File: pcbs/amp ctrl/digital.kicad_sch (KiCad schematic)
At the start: 97 parts, among them J14 RF_Shield_Two_Pieces, U11 LT1880, U12 74LVC1G04, U6 LTC6220/LT6202, U8 AD5676, U90 ADS8168/ADS8167

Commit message: Backplane comms updates, manufacturing renaming
Removed misspelled "maunfacturing" folder, fixed gitignore rule to remove manufacturing folders within individual PCB folders too
Changed SCKI/SCKO terminology to SCK, SCK_LB (loopback) for clarity
Added ADC_CS loopback signal between amp ctrl board & backplane for better fast-clock timing (#38)
Backplane: changed LVDS FPGA outputs to single-ended FPGA outputs to gain more I/O pins, added external LVDS transceivers (#38)
Backplane: replaced global clock & ~LDAC buffers with a separate FPGA pin for each amp ctrl board (#38)
Backplane: removed +2.5V power supply and level translations, no longer needed without FPGA I/O pins using LVDS_25 I/O configuration
Backplane: replaced +VDC-input resistor with solder jumper (on by default)
Backplane: changed field names (Part Number to MPN) to match Aisler's naming convention for automatic recognition
Amp ctrl: fixed optional level-shifter circuit on each channel for voltage inputs (#9) schematic & channel-1 layout
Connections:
- net ADC_SCK_LB: now reaches U12.4, U90.25 (SClk)
- net ADC_SCKI renamed ADC_SCK
- net DAC_SCKI renamed DAC_SCK

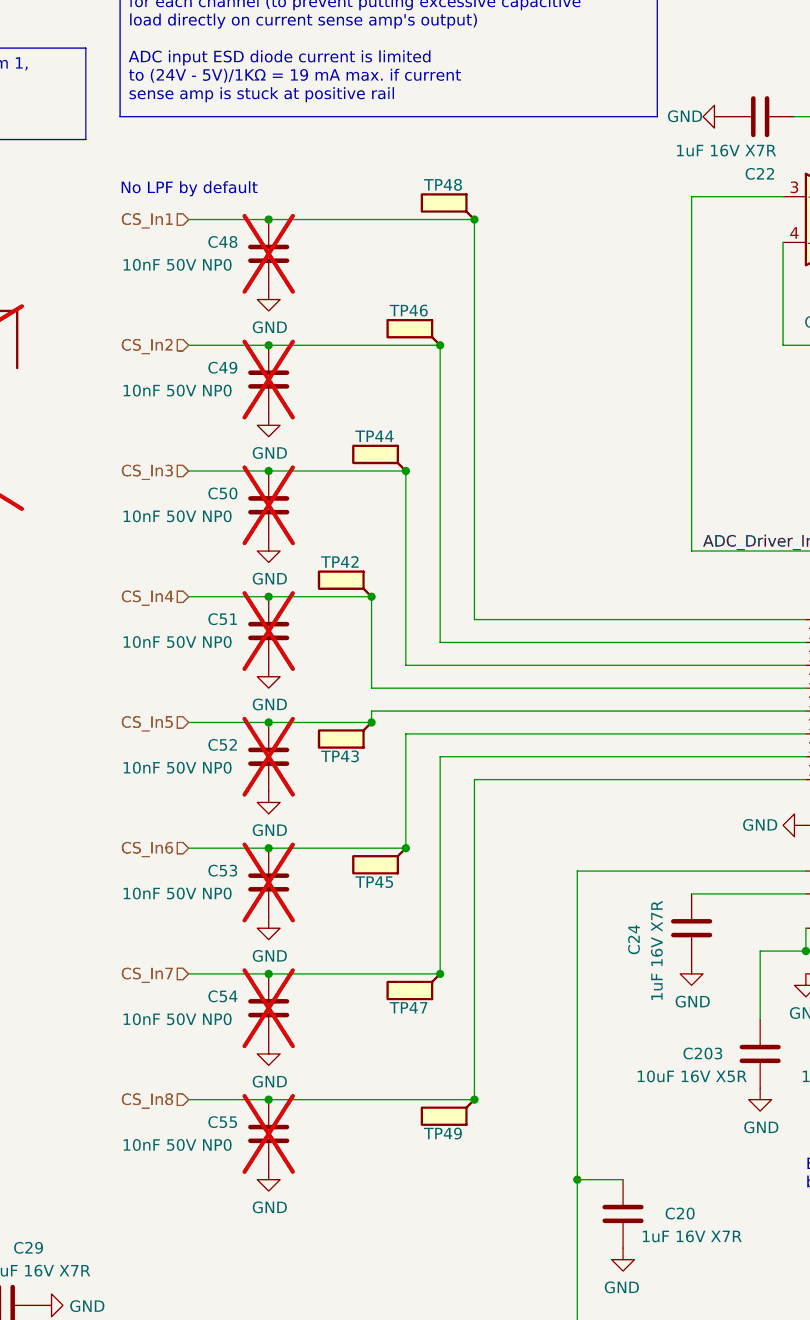
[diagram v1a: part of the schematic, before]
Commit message: Amp control board layout
Finished routing for pinout changes on backplane-to-amp-board connectors (fixes #38)
Changed ADC input testpoints back to pads (from solder-loops), as the Keystone 5019 pads didn't fit, and current sense signals can be probed at the individual channels anyways
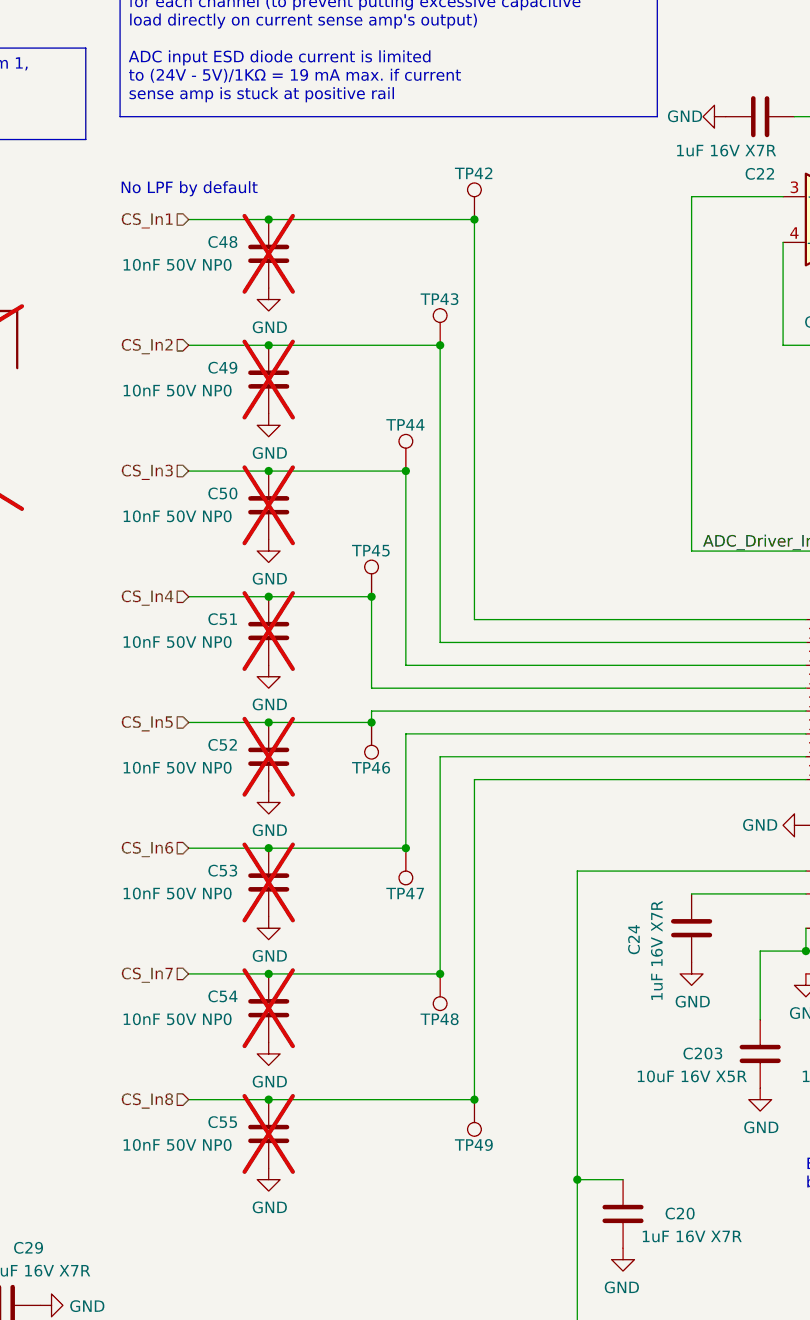
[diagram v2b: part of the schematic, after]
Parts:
- removed TP42, TP43, TP44, TP45, TP46, TP47, TP48, TP49: TestPoint_Flag, TestPoint:TestPoint_Keystone_5019_Miniature, symbol Connector:TestPoint_Flag
- added TP42, TP43, TP44, TP45, TP46, TP47, TP48, TP49: TestPoint, TestPoint:TestPoint_Pad_1.0x1.0mm, symbol Connector:TestPoint
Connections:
- net CS_In1: now also TP42.1
- net CS_In2: now also TP43.1
- net CS_In3: now also TP44.1
- net CS_In4: now also TP45.1
- net CS_In5: now also TP46.1
- net CS_In6: now also TP47.1
- net CS_In7: now also TP48.1
- net CS_In8: now also TP49.1

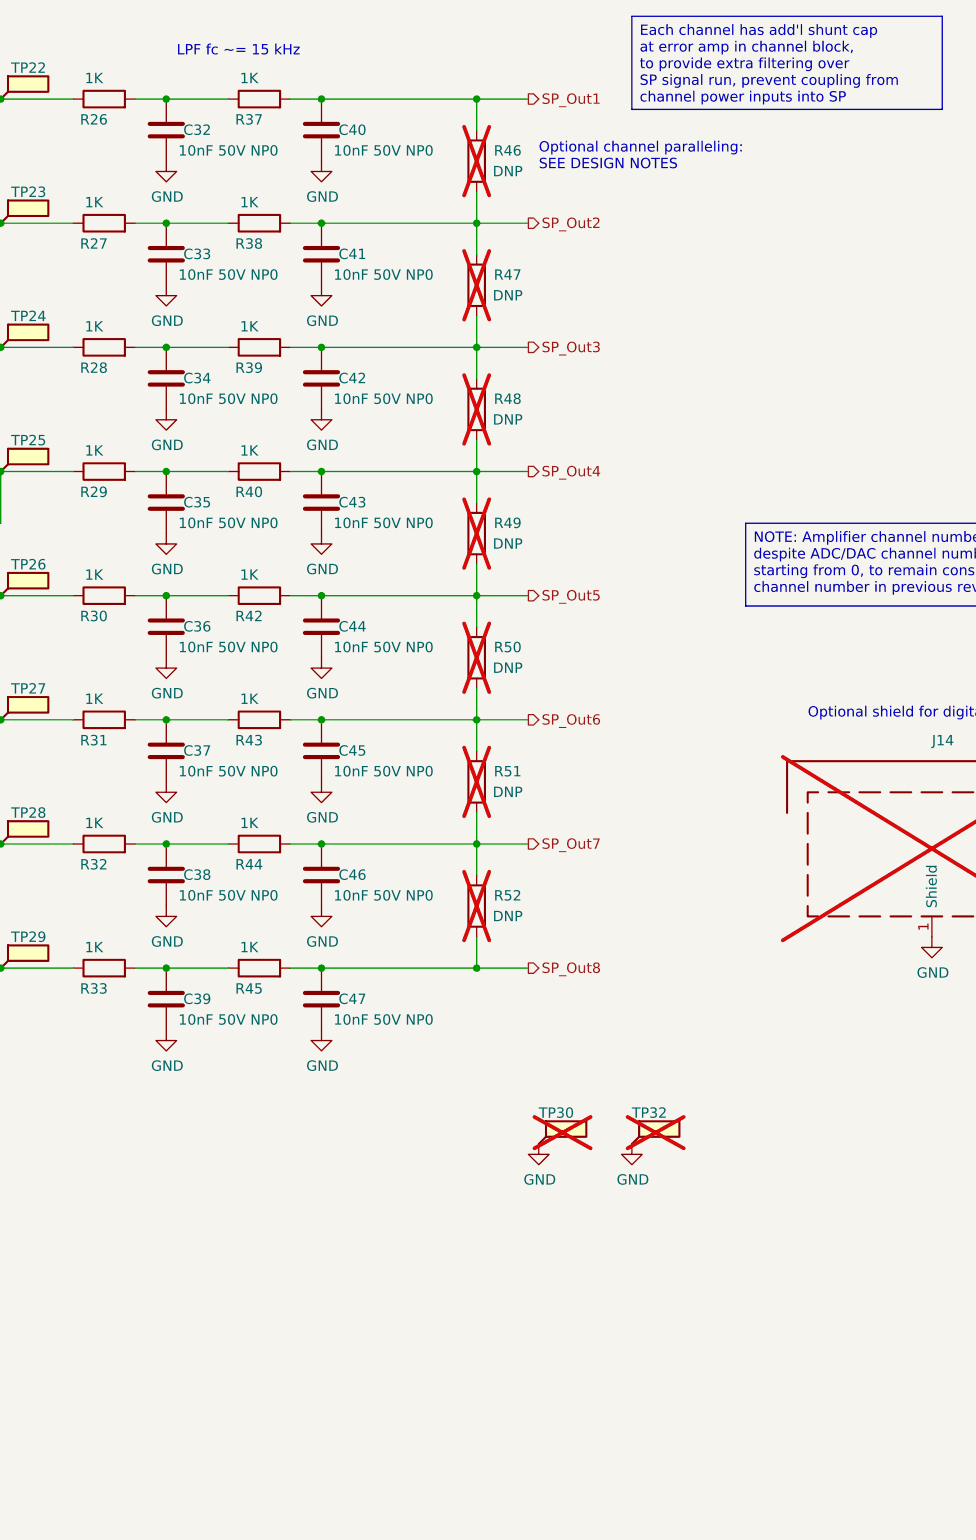
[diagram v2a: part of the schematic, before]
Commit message: Amp ctrl: DAC-filter jumpers, paralleling channels
Added jumpers to disconnect 2nd set of filter capacitors in DAC smoothing filter (fixes #42)
Extended shield footprint around digital section, no longer fits off-the-shelf part (but haven't had a reason to use it yet) to leave room for jumpers
Changed to an experimental channel-paralleling scheme (#19)
Finished copying level shifter layout to other channels (#9)
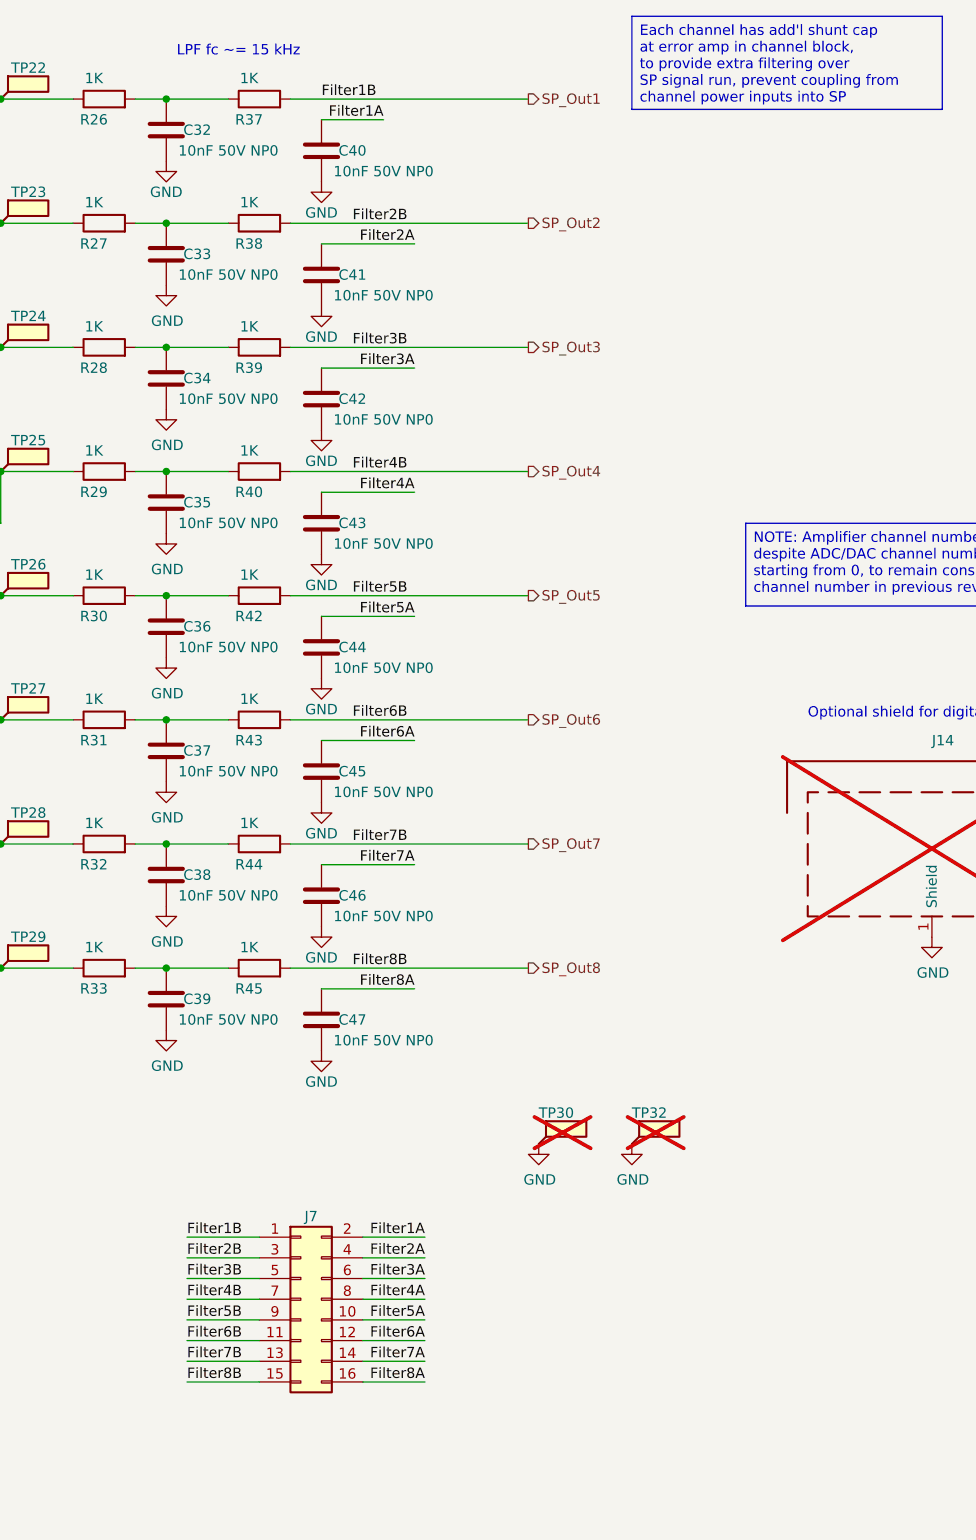
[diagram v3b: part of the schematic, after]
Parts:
- removed R46, R47, R48, R49, R50, R51, R52: DNP, Resistor_SMD:R_0805_2012Metric, symbol Device:R
- added J7: Conn_02x08_Odd_Even, Connector_PinHeader_2.54mm:PinHeader_2x08_P2.54mm_Vertical, symbol Connector_Generic:Conn_02x08_Odd_Even
- J14: footprint shim:Shield_Wurth_36107406S_Minimal-inside -> shim:Shield_44x47mm; MPN 36107406S, 36007400S -> (none); Manufacturer Wuerth -> (none)
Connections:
- net SP_Out1: now also J7.1 (Pin_1); no longer C40.2
- net SP_Out2: now also J7.3 (Pin_3); no longer C41.2
- net SP_Out3: now also J7.5 (Pin_5); no longer C42.2
- net SP_Out4: now also J7.7 (Pin_7); no longer C43.2
- net SP_Out5: now also J7.9 (Pin_9); no longer C44.2
- net SP_Out6: now also J7.11 (Pin_11); no longer C45.2
- net SP_Out7: now also J7.13 (Pin_13); no longer C46.2
- net SP_Out8: now also J7.15 (Pin_15); no longer C47.2
- new net Filter1A: C40.2, J7.2 (Pin_2)
- new net Filter2A: C41.2, J7.4 (Pin_4)
- new net Filter3A: C42.2, J7.6 (Pin_6)
- new net Filter4A: C43.2, J7.8 (Pin_8)
- new net Filter5A: C44.2, J7.10 (Pin_10)
- new net Filter6A: C45.2, J7.12 (Pin_12)
- new net Filter7A: C46.2, J7.14 (Pin_14)
- new net Filter8A: C47.2, J7.16 (Pin_16)
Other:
- note removed: "Optional channel paralleling: SEE DESIGN NOTES"
- moved on the sheet: C40, C41, C42, C43, C44, C45, C46, C47
